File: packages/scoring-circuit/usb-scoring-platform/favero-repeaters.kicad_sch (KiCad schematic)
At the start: 14 parts, among them J10 5520250-2, J9 5520250-2, Q3 BSS138-7-F, U16 4N32M, U17 4N32M

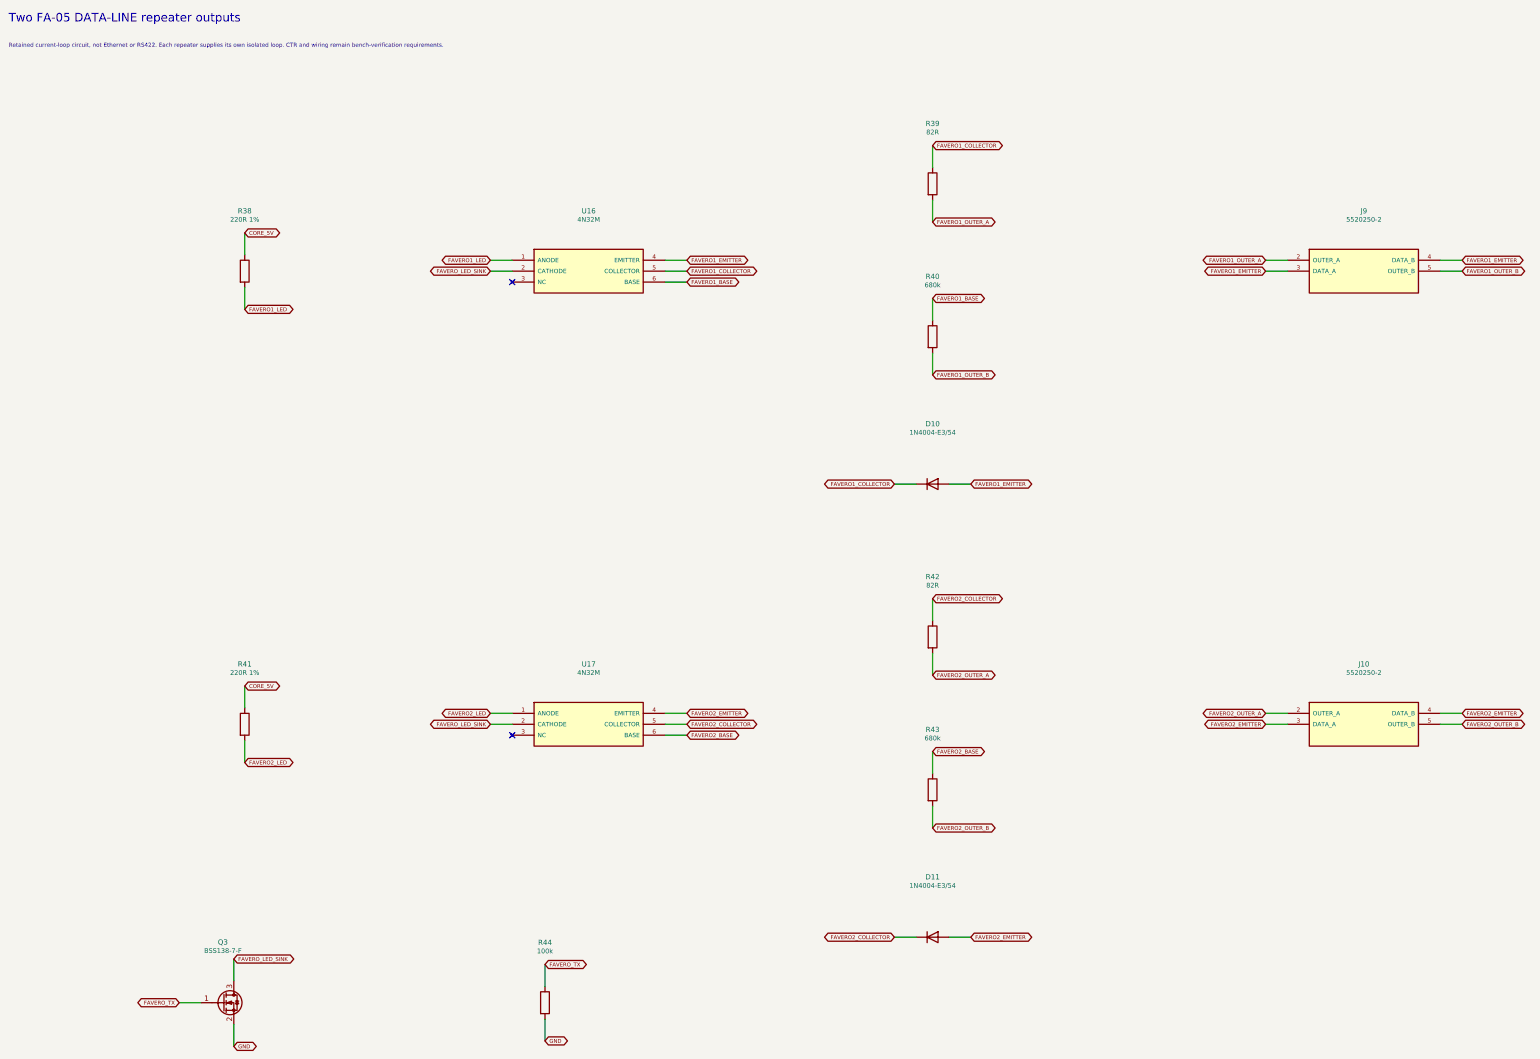
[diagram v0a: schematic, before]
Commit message: fix(scoring-circuit): correct and route isolated Favero outputs
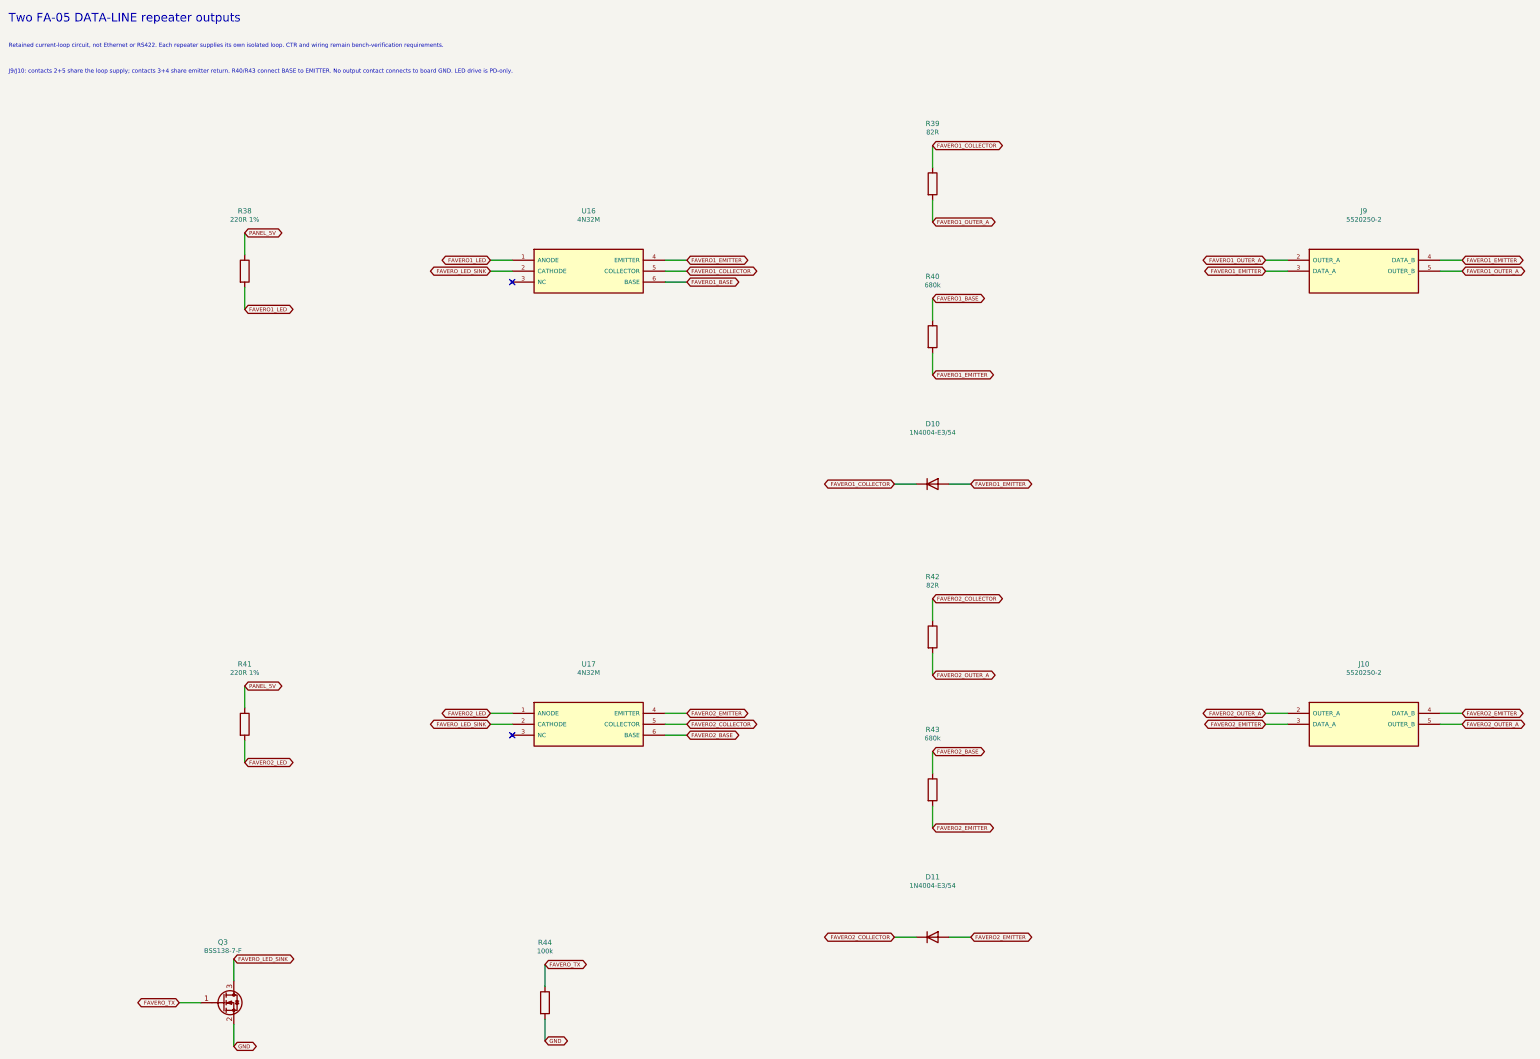
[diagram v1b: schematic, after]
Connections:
- net FAVERO1_EMITTER: now also R40.2
- net FAVERO1_OUTER_A: now also J9.5 (OUTER_B)
- net FAVERO2_EMITTER: now also R43.2
- net FAVERO2_OUTER_A: now also J10.5 (OUTER_B)
- net CORE_5V renamed PANEL_5V
- removed net FAVERO1_OUTER_B: J9.5 (OUTER_B), R40.2
- removed net FAVERO2_OUTER_B: J10.5 (OUTER_B), R43.2
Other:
- note added: "J9/J10: contacts 2+5 share the loop supply; contacts 3+4 share emitter return. R40/R43 connect BASE to EMITTER. No output contact connects to board GND. LED drive is PD-only."

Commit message: feat(scoring-circuit): select exact prototype resistor parts
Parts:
- R38, R41: MPN (none) -> ERJPA3F2200V; Manufacturer (none) -> Panasonic
- R39, R42: MPN (none) -> ERJPA3F82R0V; Manufacturer (none) -> Panasonic
- R40, R43: MPN (none) -> RC0603FR-07680KL; Manufacturer (none) -> YAGEO
- R44: MPN (none) -> RC0603FR-07100KL; Manufacturer (none) -> YAGEO

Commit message: feat(scoring-circuit): bind diode selections and review polarity
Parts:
- D10, D11: MPN (none) -> 1N4004-E3/54; Manufacturer (none) -> Vishay
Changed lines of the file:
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@@
 (wire (pts (xy 234.95 93.98) (xy 234.95 99.06)) (stroke (width 0) (type default)))
 (global_label "FAVERO1_EMITTER" (shape bidirectional) (at 234.95 99.06 0) (effects (font (size 0.9 0.9)) (justify left)) (property "Intersheetrefs" "" (at 234.95 99.06 0) (effects (font (size 1 1)) (hide yes))))
-(symbol (lib_id "Device:D") (at 234.95 124.46 0) (unit 1) (in_bom yes) (on_board yes) (dnp no) (property "Reference" "D10" (at 234.95 110.46 0) (effects (font (size 1.2 1.2)))) (property "Value" "1N4004-E3/54" (at 234.95 112.46 0) (effects (font (size 1.1 1.1)))) (property "Footprint" "Diode_THT:D_DO-41_SOD81_P10.16mm_Horizontal" (at 234.95 124.46 0) (effects (font (size 1 1)) (hide yes))) (pin "1") (pin "2") (instances (project "usb-scoring-platform" (path "/20cc8167-128c-446a-a106-f942323e143f/19a689f6-051a-47d6-a064-26f29b455422" (reference "D10") (unit 1)))))
+(symbol (lib_id "Device:D") (at 234.95 124.46 0) (unit 1) (in_bom yes) (on_board yes) (dnp no) (property "Reference" "D10" (at 234.95 110.46 0) (effects (font (size 1.2 1.2)))) (property "Value" "1N4004-E3/54" (at 234.95 112.46 0) (effects (font (size 1.1 1.1)))) (property "Footprint" "Diode_THT:D_DO-41_SOD81_P10.16mm_Horizontal" (at 234.95 124.46 0) (effects (font (size 1 1)) (hide yes))) (pin "1") (pin "2") (property "Manufacturer" "Vishay" (at 0 0 0) (effects (font (size 1 1)) (hide yes))) (property "MPN" "1N4004-E3/54" (at 0 0 0) (effects (font (size 1 1)) (hide yes))) (property "Datasheet" "https://www.vishay.com/docs/88503/1n4001.pdf" (at 0 0 0) (effects (font (size 1 1)) (hide yes))) (instances (project "usb-scoring-platform" (path "/20cc8167-128c-446a-a106-f942323e143f/19a689f6-051a-47d6-a064-26f29b455422" (reference "D10") (unit 1)))))
 (wire (pts (xy 231.14 124.46) (xy 226.06 124.46)) (stroke (width 0) (type default)))
 (global_label "FAVERO1_COLLECTOR" (shape bidirectional) (at 226.06 124.46 180) (effects (font (size 0.9 0.9)) (justify right)) (property "Intersheetrefs" "" (at 226.06 124.46 180) (effects (font (size 1 1)) (hide yes))))
@@
 (wire (pts (xy 234.95 199.39) (xy 234.95 204.47)) (stroke (width 0) (type default)))
 (global_label "FAVERO2_EMITTER" (shape bidirectional) (at 234.95 204.47 0) (effects (font (size 0.9 0.9)) (justify left)) (property "Intersheetrefs" "" (at 234.95 204.47 0) (effects (font (size 1 1)) (hide yes))))
-(symbol (lib_id "Device:D") (at 234.95 229.87 0) (unit 1) (in_bom yes) (on_board yes) (dnp no) (property "Reference" "D11" (at 234.95 215.87 0) (effects (font (size 1.2 1.2)))) (property "Value" "1N4004-E3/54" (at 234.95 217.87 0) (effects (font (size 1.1 1.1)))) (property "Footprint" "Diode_THT:D_DO-41_SOD81_P10.16mm_Horizontal" (at 234.95 229.87 0) (effects (font (size 1 1)) (hide yes))) (pin "1") (pin "2") (instances (project "usb-scoring-platform" (path "/20cc8167-128c-446a-a106-f942323e143f/19a689f6-051a-47d6-a064-26f29b455422" (reference "D11") (unit 1)))))
+(symbol (lib_id "Device:D") (at 234.95 229.87 0) (unit 1) (in_bom yes) (on_board yes) (dnp no) (property "Reference" "D11" (at 234.95 215.87 0) (effects (font (size 1.2 1.2)))) (property "Value" "1N4004-E3/54" (at 234.95 217.87 0) (effects (font (size 1.1 1.1)))) (property "Footprint" "Diode_THT:D_DO-41_SOD81_P10.16mm_Horizontal" (at 234.95 229.87 0) (effects (font (size 1 1)) (hide yes))) (pin "1") (pin "2") (property "Manufacturer" "Vishay" (at 0 0 0) (effects (font (size 1 1)) (hide yes))) (property "MPN" "1N4004-E3/54" (at 0 0 0) (effects (font (size 1 1)) (hide yes))) (property "Datasheet" "https://www.vishay.com/docs/88503/1n4001.pdf" (at 0 0 0) (effects (font (size 1 1)) (hide yes))) (instances (project "usb-scoring-platform" (path "/20cc8167-128c-446a-a106-f942323e143f/19a689f6-051a-47d6-a064-26f29b455422" (reference "D11") (unit 1)))))
 (wire (pts (xy 231.14 229.87) (xy 226.06 229.87)) (stroke (width 0) (type default)))
 (global_label "FAVERO2_COLLECTOR" (shape bidirectional) (at 226.06 229.87 180) (effects (font (size 0.9 0.9)) (justify right)) (property "Intersheetrefs" "" (at 226.06 229.87 180) (effects (font (size 1 1)) (hide yes))))

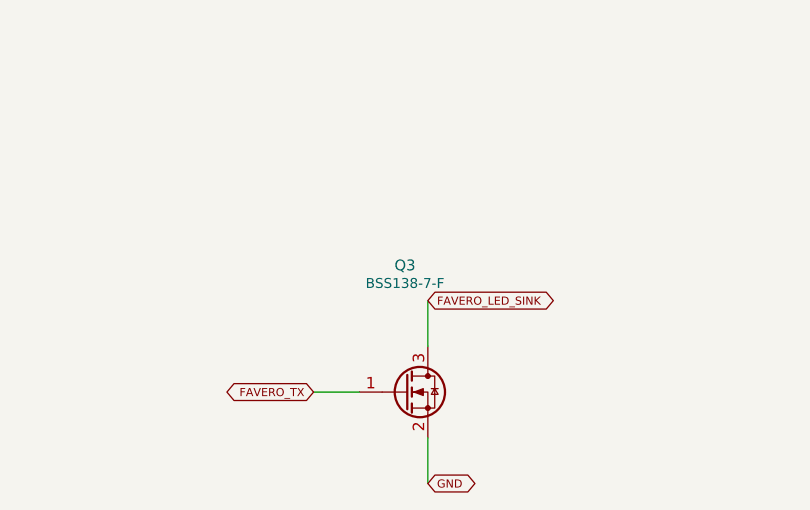
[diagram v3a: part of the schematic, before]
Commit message: fix(scoring-circuit): select low-voltage switching transistors
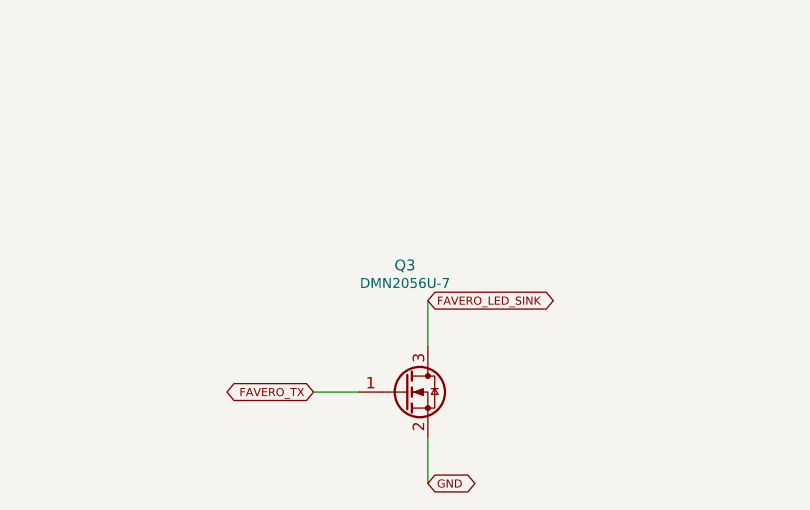
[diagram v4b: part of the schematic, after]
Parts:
- Q3: value BSS138-7-F -> DMN2056U-7; MPN (none) -> DMN2056U-7; Manufacturer (none) -> Diodes Incorporated
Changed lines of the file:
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@@
 (wire (pts (xy 238.76 229.87) (xy 243.84 229.87)) (stroke (width 0) (type default)))
 (global_label "FAVERO2_EMITTER" (shape bidirectional) (at 243.84 229.87 0) (effects (font (size 0.9 0.9)) (justify left)) (property "Intersheetrefs" "" (at 243.84 229.87 0) (effects (font (size 1 1)) (hide yes))))
-(symbol (lib_id "Transistor_FET:BSS138") (at 69.85 245.11 0) (unit 1) (in_bom yes) (on_board yes) (dnp no) (property "Reference" "Q3" (at 69.85 231.03 0) (effects (font (size 1.2 1.2)))) (property "Value" "BSS138-7-F" (at 69.85 233.03 0) (effects (font (size 1.1 1.1)))) (property "Footprint" "Package_TO_SOT_SMD:SOT-23" (at 69.85 245.11 0) (effects (font (size 1 1)) (hide yes))) (pin "1") (pin "2") (pin "3") (instances (project "usb-scoring-platform" (path "/20cc8167-128c-446a-a106-f942323e143f/19a689f6-051a-47d6-a064-26f29b455422" (reference "Q3") (unit 1)))))
+(symbol (lib_id "Transistor_FET:BSS138") (at 69.85 245.11 0) (unit 1) (in_bom yes) (on_board yes) (dnp no) (property "Reference" "Q3" (at 69.85 231.03 0) (effects (font (size 1.2 1.2)))) (property "Value" "DMN2056U-7" (at 69.85 233.03 0) (effects (font (size 1.1 1.1)))) (property "Footprint" "Package_TO_SOT_SMD:SOT-23" (at 69.85 245.11 0) (effects (font (size 1 1)) (hide yes))) (pin "1") (pin "2") (pin "3") (instances (project "usb-scoring-platform" (path "/20cc8167-128c-446a-a106-f942323e143f/19a689f6-051a-47d6-a064-26f29b455422" (reference "Q3") (unit 1)))) (property "Manufacturer" "Diodes Incorporated" (at 0 0 0) (effects (font (size 1 1)) (hide yes))) (property "MPN" "DMN2056U-7" (at 0 0 0) (effects (font (size 1 1)) (hide yes))) (property "Datasheet" "https://www.diodes.com/datasheet/download/DMN2056U.pdf" (at 0 0 0) (effects (font (size 1 1)) (hide yes))))
 (wire (pts (xy 64.77 245.11) (xy 59.69 245.11)) (stroke (width 0) (type default)))
 (global_label "FAVERO_TX" (shape bidirectional) (at 59.69 245.11 180) (effects (font (size 0.9 0.9)) (justify right)) (property "Intersheetrefs" "" (at 59.69 245.11 180) (effects (font (size 1 1)) (hide yes))))
